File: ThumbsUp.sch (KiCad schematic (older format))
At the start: 153 parts, among them IC1 RP2040, IC2 W25Q128JVSIM, J1 Conn_01x04_Male, J10 Raiser_Male, J11 Raiser_Female, J12 Raiser_Male, J13 Raiser_Female, J14 Raiser_Male, J15 Raiser_Female, J16 Raiser_Male, J17 Raiser_Female, J18 Raiser_Male, J19 52559-1233, J2 Conn_01x04_Male, J20 Conn_01x04_Female, J21 Conn_01x04_Female, J22 Conn_01x04_Female, J23 Conn_01x04_Female, J24 Conn_01x04_Male, J25 Conn_01x04_Male, J26 Conn_01x04_Male, J27 Conn_01x04_Male, J28 Conn_01x04_Female, J29 Conn_01x04_Female, J3 Conn_01x04_Female, J30 Conn_01x04_Female, J31 Conn_01x04_Female, J32 USB_C_Receptacle_USB2.0, J33 STX-3501-3N, J4 Conn_01x04_Male, J5 Conn_01x04_Female, J6 Conn_01x04_Male, J7 Conn_01x04_Male, J8 Conn_01x04_Male, J9 Raiser_Female, U1 NCP1117-3.3_SOT223, Y1 ABLS-12.000MHZ-B4-T

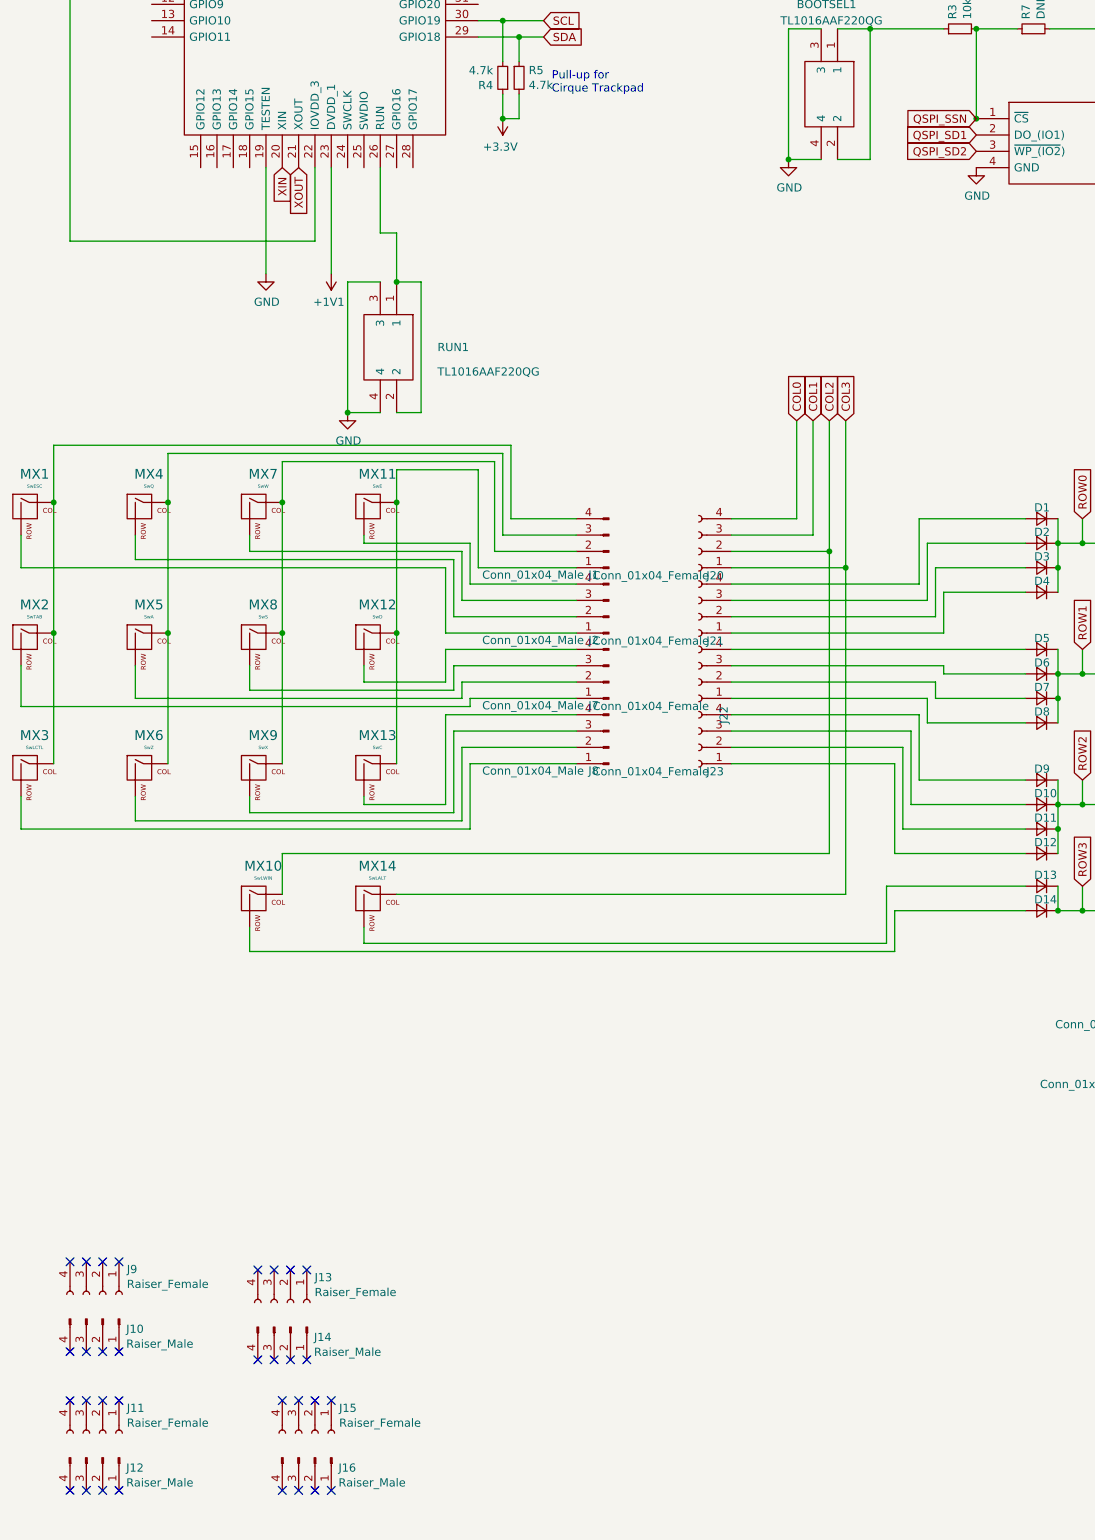
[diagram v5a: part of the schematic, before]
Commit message: Retraced the lower PCB
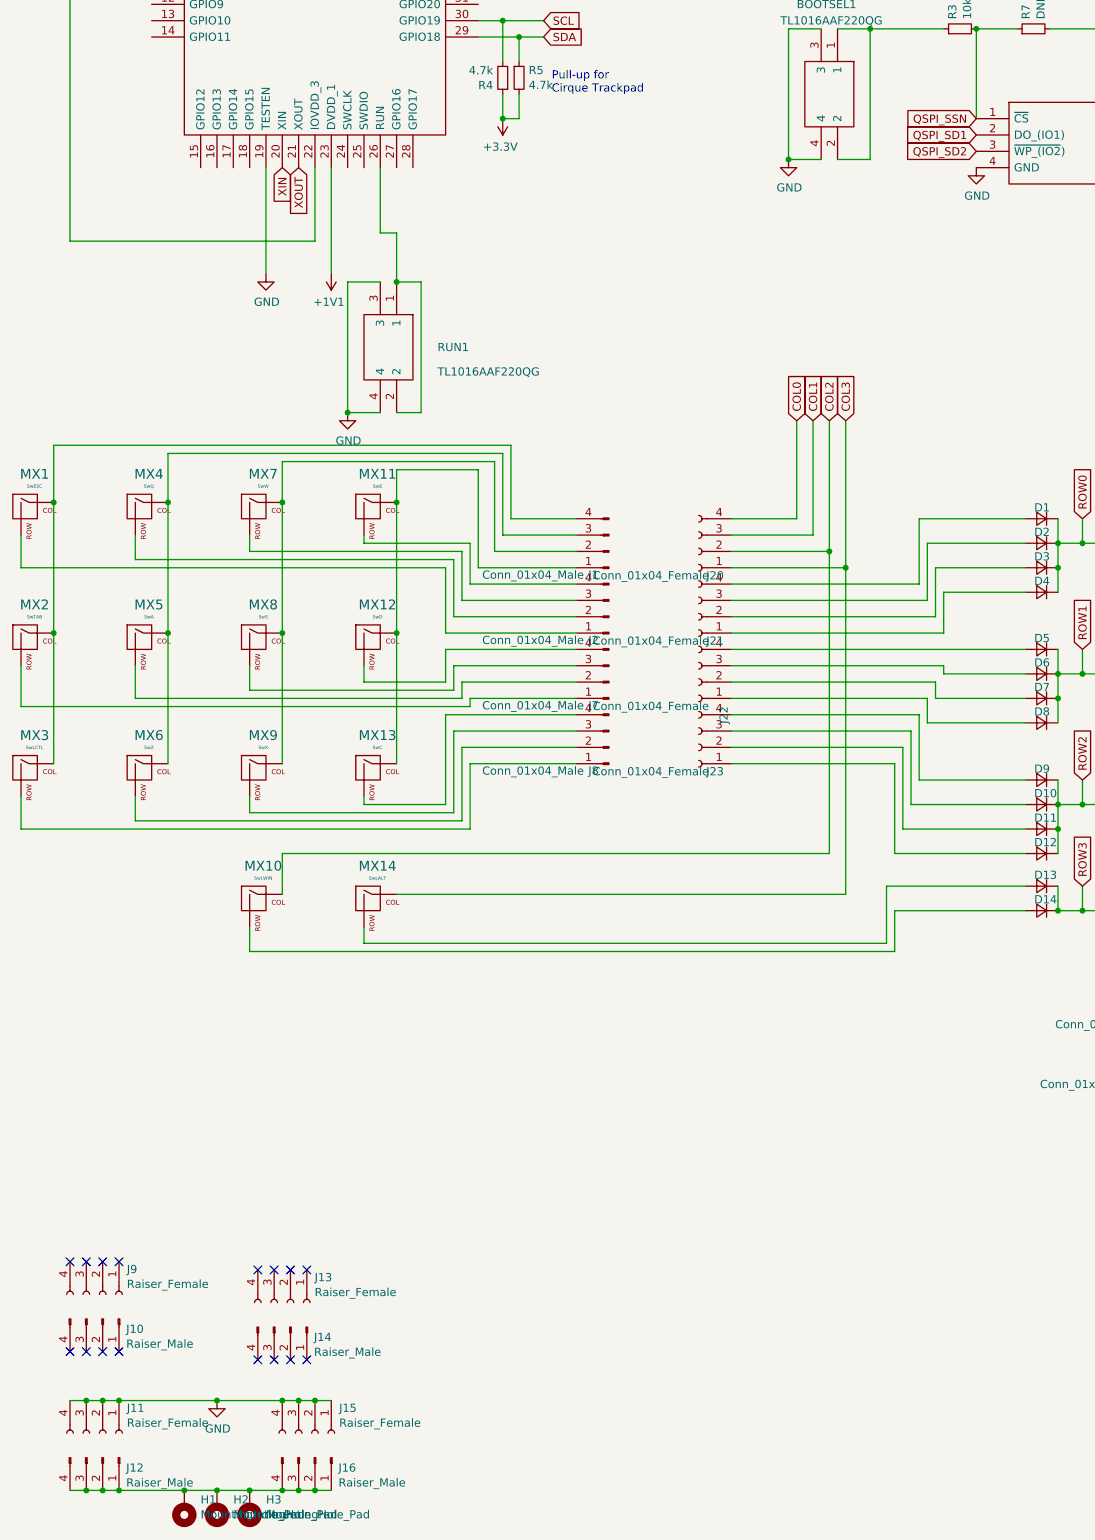
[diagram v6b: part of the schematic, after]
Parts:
- added H1, H2, H3: MountingHole_Pad, MountingHole:MountingHole_6.4mm_M6_Pad_Via, symbol Mechanical:MountingHole_Pad
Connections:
- wire segments 483 -> 501
- no-connect marks 46 -> 30
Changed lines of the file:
@@
 As in Planck/rev4:\n\n#define MATRIX_ROW_PINS { D3, D5, B5, B6 }\n#define MATRIX_COL_PINS { F1, F0, B0, C7, F4, F5, F6, F7, D4, D6, B4, D7 }\n\n#define DIODE_DIRECTION COL2ROW\n
-$Comp
-L Connector:Conn_01x04_Female J11
-U 1 1 6206CD49
-P 1750 12400
-F 0 "J11" V 1596 12548 50  0000 L CNN
-F 1 "Raiser_Female" V 1687 12548 50  0000 L CNN
-F 2 "Connector_PinSocket_2.54mm:PinSocket_1x04_P2.54mm_Vertical" H 1750 12400 50  0001 C CNN
-F 3 "~" H 1750 12400 50  0001 C CNN
-	1    1750 12400
-	0    1    1    0
-$EndComp
 $Comp
 L Connector:Conn_01x04_Male J12
@@
 	0    1    1    0
 $EndComp
-NoConn ~ 1550 12200
-NoConn ~ 1650 12200
-NoConn ~ 1750 12200
-NoConn ~ 1850 12200
-NoConn ~ 1550 12750
-NoConn ~ 1650 12750
-NoConn ~ 1750 12750
-NoConn ~ 1850 12750
 $Comp
 L Connector:Conn_01x04_Female J9
@@
 NoConn ~ 2900 11950
 NoConn ~ 3000 11950
-$Comp
-L Connector:Conn_01x04_Female J15
-U 1 1 6225ECEC
-P 3050 12400
-F 0 "J15" V 2896 12548 50  0000 L CNN
-F 1 "Raiser_Female" V 2987 12548 50  0000 L CNN
-F 2 "Connector_PinSocket_2.54mm:PinSocket_1x04_P2.54mm_Vertical" H 3050 12400 50  0001 C CNN
-F 3 "~" H 3050 12400 50  0001 C CNN
-	1    3050 12400
-	0    1    1    0
-$EndComp
-$Comp
-L Connector:Conn_01x04_Male J16
-U 1 1 6225ECF6
-P 3050 12550
-F 0 "J16" V 3112 12694 50  0000 L CNN
-F 1 "Raiser_Male" V 3203 12694 50  0000 L CNN
-F 2 "Connector_PinHeader_2.54mm:PinHeader_1x04_P2.54mm_Vertical" H 3050 12550 50  0001 C CNN
-F 3 "~" H 3050 12550 50  0001 C CNN
-	1    3050 12550
-	0    1    1    0
-$EndComp
-NoConn ~ 2850 12200
-NoConn ~ 2950 12200
-NoConn ~ 3050 12200
-NoConn ~ 3150 12200
-NoConn ~ 2850 12750
-NoConn ~ 2950 12750
-NoConn ~ 3050 12750
-NoConn ~ 3150 12750
 $Comp
 L Connector:Conn_01x04_Female J17
@@
 Wire Wire Line
 	7100 3800 7350 3800
-Connection ~ 7100 4350
 Text GLabel 9300 4650 2    50   Input ~ 0
 QSPI_SD0
@@
 $EndComp
 Connection ~ 7100 3800
+$Comp
+L Connector:Conn_01x04_Female J11
+U 1 1 6206CD49
+P 1750 12400
+F 0 "J11" V 1596 12548 50  0000 L CNN
+F 1 "Raiser_Female" V 1687 12548 50  0000 L CNN
+F 2 "Connector_PinSocket_2.54mm:PinSocket_1x04_P2.54mm_Vertical" H 1750 12400 50  0001 C CNN
+F 3 "~" H 1750 12400 50  0001 C CNN
+	1    1750 12400
+	0    1    1    0
+$EndComp
+$Comp
+L Connector:Conn_01x04_Female J15
+U 1 1 6225ECEC
+P 3050 12400
+F 0 "J15" V 2896 12548 50  0000 L CNN
+F 1 "Raiser_Female" V 2987 12548 50  0000 L CNN
+F 2 "Connector_PinSocket_2.54mm:PinSocket_1x04_P2.54mm_Vertical" H 3050 12400 50  0001 C CNN
+F 3 "~" H 3050 12400 50  0001 C CNN
+	1    3050 12400
+	0    1    1    0
+$EndComp
+$Comp
+L Connector:Conn_01x04_Male J16
+U 1 1 6225ECF6
+P 3050 12550
+F 0 "J16" V 3112 12694 50  0000 L CNN
+F 1 "Raiser_Male" V 3203 12694 50  0000 L CNN
+F 2 "Connector_PinHeader_2.54mm:PinHeader_1x04_P2.54mm_Vertical" H 3050 12550 50  0001 C CNN
+F 3 "~" H 3050 12550 50  0001 C CNN
+	1    3050 12550
+	0    1    1    0
+$EndComp
+Wire Wire Line
+	1550 12750 1650 12750
+Connection ~ 1650 12750
+Wire Wire Line
+	1650 12750 1750 12750
+Connection ~ 1750 12750
+Wire Wire Line
+	1750 12750 1850 12750
+Connection ~ 1850 12750
+Wire Wire Line
+	1850 12750 2250 12750
+Connection ~ 2850 12750
+Wire Wire Line
+	2850 12750 2950 12750
+Connection ~ 2950 12750
+Wire Wire Line
+	2950 12750 3050 12750
+Connection ~ 3050 12750
+Wire Wire Line
+	3050 12750 3150 12750
+Wire Wire Line
+	1550 12200 1650 12200
+Connection ~ 1650 12200
+Wire Wire Line
+	1650 12200 1750 12200
+Connection ~ 1750 12200
+Wire Wire Line
+	1750 12200 1850 12200
+Connection ~ 1850 12200
+Wire Wire Line
+	1850 12200 2450 12200
+Connection ~ 2850 12200
+Wire Wire Line
+	2850 12200 2950 12200
+Connection ~ 2950 12200
+Wire Wire Line
+	2950 12200 3050 12200
+Connection ~ 3050 12200
+Wire Wire Line
+	3050 12200 3150 12200
+$Comp
+L power:GND #PWR0116
+U 1 1 6438318D
+P 2450 12200
+F 0 "#PWR0116" H 2450 11950 50  0001 C CNN
+F 1 "GND" H 2455 12027 50  0000 C CNN
+F 2 "" H 2450 12200 50  0001 C CNN
+F 3 "" H 2450 12200 50  0001 C CNN
+	1    2450 12200
+	1    0    0    -1
+$EndComp
+Connection ~ 2450 12200
+Wire Wire Line
+	2450 12200 2850 12200
+$Comp
+L Mechanical:MountingHole_Pad H3
+U 1 1 6438E44E
+P 2650 12850
+F 0 "H3" H 2550 12807 50  0000 R CNN
+F 1 "MountingHole_Pad" H 2550 12898 50  0000 R CNN
+F 2 "MountingHole:MountingHole_6.4mm_M6_Pad_Via" H 2650 12850 50  0001 C CNN
+F 3 "~" H 2650 12850 50  0001 C CNN
+	1    2650 12850
+	-1   0    0    1
+$EndComp
+Connection ~ 2650 12750
+Wire Wire Line
+	2650 12750 2850 12750
+$Comp
+L Mechanical:MountingHole_Pad H2
+U 1 1 6438EF5B
+P 2450 12850
+F 0 "H2" H 2350 12807 50  0000 R CNN
+F 1 "MountingHole_Pad" H 2350 12898 50  0000 R CNN
+F 2 "MountingHole:MountingHole_6.4mm_M6_Pad_Via" H 2450 12850 50  0001 C CNN
+F 3 "~" H 2450 12850 50  0001 C CNN
+	1    2450 12850
+	-1   0    0    1
+$EndComp
+Connection ~ 2450 12750
+Wire Wire Line
+	2450 12750 2650 12750
+$Comp
+L Mechanical:MountingHole_Pad H1
+U 1 1 6438F90E
+P 2250 12850
+F 0 "H1" H 2150 12807 50  0000 R CNN
+F 1 "MountingHole_Pad" H 2150 12898 50  0000 R CNN
+F 2 "MountingHole:MountingHole_6.4mm_M6_Pad_Via" H 2250 12850 50  0001 C CNN
+F 3 "~" H 2250 12850 50  0001 C CNN
+	1    2250 12850
+	-1   0    0    1
+$EndComp
+Connection ~ 2250 12750
+Wire Wire Line
+	2250 12750 2450 12750
 $EndSCHEMATC
